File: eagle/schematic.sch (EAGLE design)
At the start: 24 parts, among them IC1 PIC18F1320SO, U1 MIC5205, U2 SG-3040LC, U3 SG-3030JC

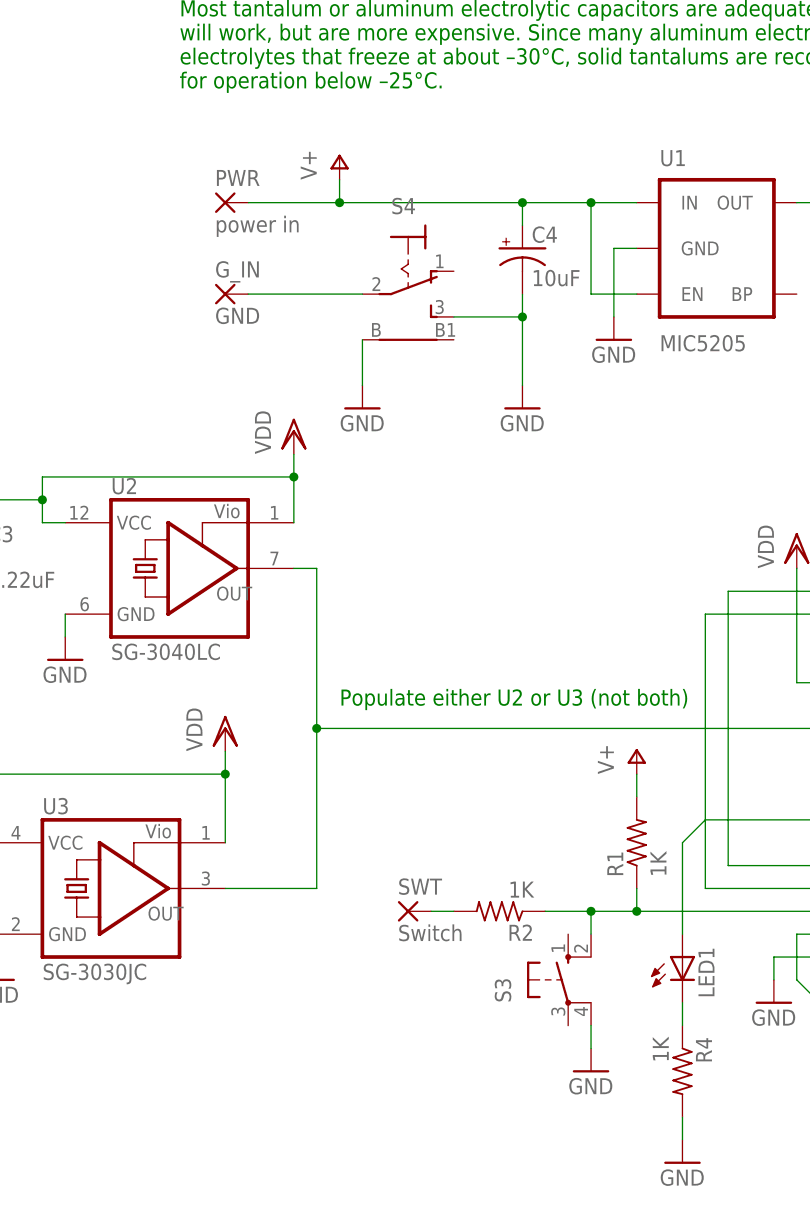
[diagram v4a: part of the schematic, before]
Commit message: Correct wiring of manual push switch, larger holes for ICD, increase U2 footprint
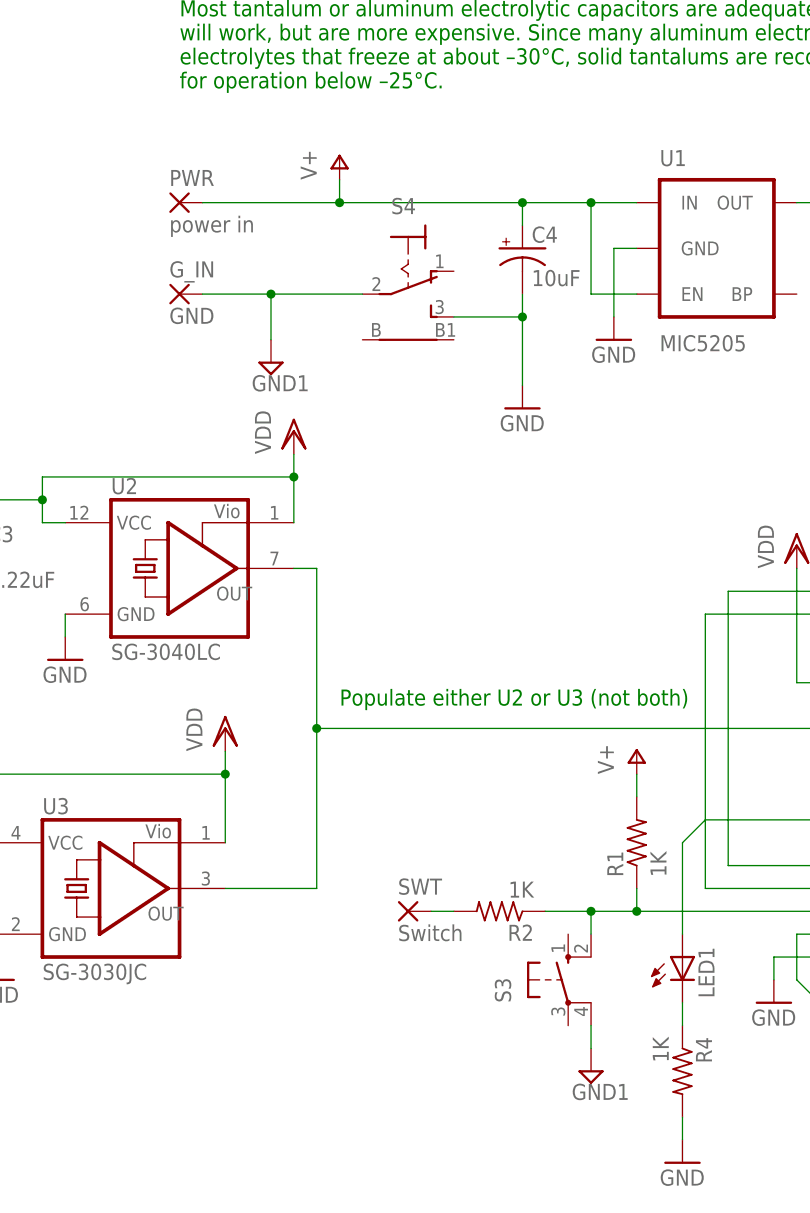
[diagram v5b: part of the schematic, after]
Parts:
- U2: device untitled:SG-3040LCLC -> untitled:SG-3030,40(LC,JC,JF)LC-LARGE
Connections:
- removed net GND: C2.2, C3.2, C4.-, C5.-, C6.2, IC1.VSS@AVSS, ICD-3.1, R4.2, S1.C, S2.C, S3.P1, S4.B, S4.S, U1.GND, U2.GND, U3.GND
- removed net SWITCHED_GND: G_IN.P, S4.P
- new net GND1: G_IN.P, S3.P1, S4.P
- new net N$12: C2.2, C3.2, C4.-, C5.-, C6.2, IC1.VSS@AVSS, ICD-3.1, R4.2, S1.C, S2.C, S4.S, U1.GND, U2.GND, U3.GND
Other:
- moved on the sheet: G_IN, PWR
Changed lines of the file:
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@@
 <grid distance="0.1" unitdist="inch" unit="inch" style="lines" multiple="1" display="no" altdistance="0.01" altunitdist="inch" altunit="inch"/>
 <layers>
-<layer number="1" name="Top" color="4" fill="1" visible="no" active="no"/>
-<layer number="16" name="Bottom" color="1" fill="1" visible="no" active="no"/>
-<layer number="17" name="Pads" color="2" fill="1" visible="no" active="no"/>
-<layer number="18" name="Vias" color="2" fill="1" visible="no" active="no"/>
-<layer number="19" name="Unrouted" color="6" fill="1" visible="no" active="no"/>
-<layer number="20" name="Dimension" color="15" fill="1" visible="no" active="no"/>
-<layer number="21" name="tPlace" color="7" fill="1" visible="no" active="no"/>
-<layer number="22" name="bPlace" color="7" fill="1" visible="no" active="no"/>
-<layer number="23" name="tOrigins" color="15" fill="1" visible="no" active="no"/>
-<layer number="24" name="bOrigins" color="15" fill="1" visible="no" active="no"/>
-<layer number="25" name="tNames" color="7" fill="1" visible="no" active="no"/>
-<layer number="26" name="bNames" color="7" fill="1" visible="no" active="no"/>
-<layer number="27" name="tValues" color="7" fill="1" visible="no" active="no"/>
-<layer number="28" name="bValues" color="7" fill="1" visible="no" active="no"/>
+<layer number="1" name="Top" color="4" fill="1" visible="yes" active="no"/>
+<layer number="16" name="Bottom" color="1" fill="1" visible="yes" active="no"/>
+<layer number="17" name="Pads" color="2" fill="1" visible="yes" active="no"/>
+<layer number="18" name="Vias" color="2" fill="1" visible="yes" active="no"/>
+<layer number="19" name="Unrouted" color="6" fill="1" visible="yes" active="no"/>
+<layer number="20" name="Dimension" color="15" fill="1" visible="yes" active="no"/>
+<layer number="21" name="tPlace" color="7" fill="1" visible="yes" active="no"/>
+<layer number="22" name="bPlace" color="7" fill="1" visible="yes" active="no"/>
+<layer number="23" name="tOrigins" color="15" fill="1" visible="yes" active="no"/>
+<layer number="24" name="bOrigins" color="15" fill="1" visible="yes" active="no"/>
+<layer number="25" name="tNames" color="7" fill="1" visible="yes" active="no"/>
+<layer number="26" name="bNames" color="7" fill="1" visible="yes" active="no"/>
+<layer number="27" name="tValues" color="7" fill="1" visible="yes" active="no"/>
+<layer number="28" name="bValues" color="7" fill="1" visible="yes" active="no"/>
 <layer number="29" name="tStop" color="7" fill="3" visible="no" active="no"/>
 <layer number="30" name="bStop" color="7" fill="6" visible="no" active="no"/>
@@
 <layer number="35" name="tGlue" color="7" fill="4" visible="no" active="no"/>
 <layer number="36" name="bGlue" color="7" fill="5" visible="no" active="no"/>
-<layer number="37" name="tTest" color="7" fill="1" visible="no" active="no"/>
-<layer number="38" name="bTest" color="7" fill="1" visible="no" active="no"/>
+<layer number="37" name="tTest" color="7" fill="1" visible="yes" active="no"/>
+<layer number="38" name="bTest" color="7" fill="1" visible="yes" active="no"/>
 <layer number="39" name="tKeepout" color="4" fill="11" visible="no" active="no"/>
 <layer number="40" name="bKeepout" color="1" fill="11" visible="no" active="no"/>
@@
 <layer number="44" name="Drills" color="7" fill="1" visible="no" active="no"/>
 <layer number="45" name="Holes" color="7" fill="1" visible="no" active="no"/>
-<layer number="46" name="Milling" color="3" fill="1" visible="no" active="no"/>
-<layer number="47" name="Measures" color="7" fill="1" visible="no" active="no"/>
-<layer number="48" name="Document" color="7" fill="1" visible="no" active="no"/>
-<layer number="49" name="Reference" color="7" fill="1" visible="no" active="no"/>
-<layer number="50" name="dxf" color="7" fill="1" visible="no" active="no"/>
-<layer number="51" name="tDocu" color="7" fill="1" visible="no" active="no"/>
-<layer number="52" name="bDocu" color="7" fill="1" visible="no" active="no"/>
-<layer number="53" name="tGND_GNDA" color="7" fill="9" visible="no" active="no"/>
-<layer number="54" name="bGND_GNDA" color="1" fill="9" visible="no" active="no"/>
-<layer number="56" name="wert" color="7" fill="1" visible="no" active="no"/>
+<layer number="46" name="Milling" color="3" fill="1" visible="yes" active="no"/>
+<layer number="47" name="Measures" color="7" fill="1" visible="yes" active="no"/>
+<layer number="48" name="Document" color="7" fill="1" visible="yes" active="no"/>
+<layer number="49" name="Reference" color="7" fill="1" visible="yes" active="no"/>
+<layer number="50" name="dxf" color="7" fill="1" visible="yes" active="no"/>
+<layer number="51" name="tDocu" color="7" fill="1" visible="yes" active="no"/>
+<layer number="52" name="bDocu" color="7" fill="1" visible="yes" active="no"/>
+<layer number="53" name="tGND_GNDA" color="7" fill="9" visible="yes" active="no"/>
+<layer number="54" name="bGND_GNDA" color="1" fill="9" visible="yes" active="no"/>
+<layer number="56" name="wert" color="7" fill="1" visible="yes" active="no"/>
 <layer number="90" name="Modules" color="5" fill="1" visible="yes" active="yes"/>
 <layer number="91" name="Nets" color="2" fill="1" visible="yes" active="yes"/>
@@
 <part name="S1" library="switch-dil" deviceset="P101" device=""/>
 <part name="S2" library="switch-dil" deviceset="P101" device=""/>
-<part name="U2" library="untitled" deviceset="SG-3040LC" device="LC" value="SG-3040LC"/>
+<part name="U2" library="untitled" deviceset="SG-3030,40(LC,JC,JF)" device="LC-LARGE" value="SG-3040LC"/>
 <part name="GND3" library="supply1" deviceset="GND" device=""/>
 <part name="C3" library="capacitor-wima" deviceset="C" device="2,5-3" value="0.22uF"/>
@@
 <part name="U1" library="SparkFun" deviceset="V_REG_LDO" device="SMD" value="MIC5205"/>
 <part name="LED1" library="Testing" deviceset="LED" device="3MM"/>
-<part name="GND9" library="supply1" deviceset="GND" device=""/>
 <part name="VDD4" library="supply1" deviceset="VDD" device=""/>
 <part name="GND10" library="supply1" deviceset="GND" device=""/>
@@
 <part name="VDD7" library="supply1" deviceset="VDD" device=""/>
 <part name="VDD8" library="supply1" deviceset="VDD" device=""/>
-<part name="GND7" library="supply1" deviceset="GND" device=""/>
 <part name="ICD" library="untitled" deviceset="?4B-ZR" device="B"/>
 <part name="VDD9" library="supply1" deviceset="VDD" device=""/>
 <part name="GND13" library="supply1" deviceset="GND" device=""/>
 <part name="U3" library="untitled" deviceset="SG-3030,40(LC,JC,JF)" device="JC" value="SG-3030JC"/>
+<part name="SUPPLY1" library="supply2" deviceset="GND1" device=""/>
+<part name="SUPPLY2" library="supply2" deviceset="GND1" device=""/>
 </parts>
 <sheets>
@@
 <instance part="GND1" gate="1" x="30.48" y="99.06"/>
 <instance part="GND2" gate="1" x="58.42" y="33.02"/>
-<instance part="PWR" gate="1" x="-2.54" y="121.92"/>
-<instance part="G_IN" gate="1" x="-2.54" y="111.76"/>
+<instance part="PWR" gate="1" x="-7.62" y="121.92"/>
+<instance part="G_IN" gate="1" x="-7.62" y="111.76"/>
 <instance part="SWT" gate="1" x="17.78" y="43.18"/>
 <instance part="S1" gate="1" x="114.3" y="104.14" rot="R270"/>
@@
 <instance part="U1" gate="G$1" x="53.34" y="116.84"/>
 <instance part="LED1" gate="G$1" x="48.26" y="38.1"/>
-<instance part="GND9" gate="1" x="38.1" y="25.4"/>
 <instance part="VDD4" gate="G$1" x="162.56" y="68.58"/>
 <instance part="GND10" gate="1" x="162.56" y="43.18"/>
@@
 <instance part="VDD7" gate="G$1" x="71.12" y="96.52"/>
 <instance part="VDD8" gate="G$1" x="81.28" y="96.52"/>
-<instance part="GND7" gate="1" x="12.7" y="99.06"/>
 <instance part="ICD" gate="-5" x="175.26" y="50.8"/>
 <instance part="ICD" gate="-1" x="175.26" y="60.96"/>
@@
 <instance part="GND13" gate="1" x="-27.94" y="35.56"/>
 <instance part="U3" gate="G$1" x="-15.24" y="45.72"/>
+<instance part="SUPPLY1" gate="G$1" x="2.54" y="104.14"/>
+<instance part="SUPPLY2" gate="G$1" x="38.1" y="25.4"/>
 </instances>
 <busses>
 </busses>
 <nets>
-<net name="GND" class="0">
+<net name="N$12" class="0">
 <segment>
 <pinref part="IC1" gate="G$1" pin="VSS@AVSS"/>
@@
 </segment>
 <segment>
-<pinref part="GND9" gate="1" pin="GND"/>
-<pinref part="S3" gate="1" pin="P1"/>
-<wire x1="38.1" y1="30.48" x2="38.1" y2="27.94" width="0.1524" layer="91"/>
-</segment>
-<segment>
 <pinref part="GND10" gate="1" pin="GND"/>
 <wire x1="162.56" y1="55.88" x2="162.56" y2="45.72" width="0.1524" layer="91"/>
@@
 <pinref part="S1" gate="1" pin="C"/>
 <wire x1="99.06" y1="104.14" x2="106.68" y2="104.14" width="0.1524" layer="91"/>
-</segment>
-<segment>
-<pinref part="S4" gate="2" pin="B"/>
-<pinref part="GND7" gate="1" pin="GND"/>
-<wire x1="12.7" y1="106.68" x2="12.7" y2="101.6" width="0.1524" layer="91"/>
 </segment>
 <segment>
@@
 <wire x1="10.16" y1="124.46" x2="10.16" y2="121.92" width="0.1524" layer="91"/>
 <pinref part="PWR" gate="1" pin="P"/>
-<wire x1="0" y1="121.92" x2="10.16" y2="121.92" width="0.1524" layer="91"/>
+<wire x1="-5.08" y1="121.92" x2="10.16" y2="121.92" width="0.1524" layer="91"/>
 <junction x="10.16" y="121.92"/>
 <pinref part="C4" gate="G$1" pin="+"/>
@@
 </segment>
 </net>
-<net name="SWITCHED_GND" class="0">
+<net name="GND1" class="0">
 <segment>
 <pinref part="G_IN" gate="1" pin="P"/>
-<wire x1="0" y1="111.76" x2="12.7" y2="111.76" width="0.1524" layer="91"/>
+<wire x1="-5.08" y1="111.76" x2="2.54" y2="111.76" width="0.1524" layer="91"/>
 <pinref part="S4" gate="2" pin="P"/>
-</segment>
-</net>
+<junction x="2.54" y="111.76"/>
+<wire x1="2.54" y1="111.76" x2="12.7" y2="111.76" width="0.1524" layer="91"/>
+<pinref part="SUPPLY1" gate="G$1" pin="GND1"/>
+<wire x1="2.54" y1="106.68" x2="2.54" y2="111.76" width="0.1524" layer="91"/>
+</segment>
+<segment>
+<pinref part="SUPPLY2" gate="G$1" pin="GND1"/>
+<pinref part="S3" gate="1" pin="P1"/>
+<wire x1="38.1" y1="27.94" x2="38.1" y2="30.48" width="0.1524" layer="91"/>
+</segment>
+</net>

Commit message: Create new set of gerber files
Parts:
- R4: value 1K -> 523R
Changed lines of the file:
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@@
 <part name="R3" library="resistor" deviceset="R-US_" device="0204/2V" value="4.7K"/>
 <part name="VDD5" library="supply1" deviceset="VDD" device=""/>
-<part name="R4" library="resistor" deviceset="R-US_" device="0204/2V" value="1K"/>
+<part name="R4" library="resistor" deviceset="R-US_" device="0204/2V" value=" 523R"/>
 <part name="GND11" library="supply1" deviceset="GND" device=""/>
 <part name="GND12" library="supply1" deviceset="GND" device=""/>
